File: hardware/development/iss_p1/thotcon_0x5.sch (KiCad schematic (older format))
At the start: 69 parts, among them J1 POWER, J2 ANALOG, J3 DIGITAL_0, J4 DIGITAL_1, J5 EXT_POWER, J6 USB_IN, P2 ICSP, U1 ATMEGA32U4, U2 5V, U3 3.3V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

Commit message: Apr 1 2014 Paul Reich
ANGES:
   Move R14 (2.2K TH) from add-on kit to production; USB needed on all models.

DELETIONS:
   prototype directory: Schematic obsolete. Refer instead to
   hardware/development/iss_P1/release/thotcon_0x5_SCHEM-*.pdf
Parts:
- R14: ASSY_STATUS DO NOT PLACE -> (none); Y (none) -> DO NOT PLACE
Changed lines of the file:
@@
 Sheet 1 1
 Title "BOARD, PC, THOTCON-0x05"
-Date "31 mar 2014"
+Date "1 apr 2014"
 Rev "P1"
 Comp "Workshop 88"
@@
 F 6 "CF18JT2K20" H 9150 7200 60  0001 C CNN "MFR_PN"
 F 7 ".02" H 9150 7200 60  0001 C CNN "EST_COST"
-F 8 "DO NOT PLACE" H 9150 7200 60  0001 C CNN "ASSY_STATUS"
+F 8 "DO NOT PLACE" H 9150 7200 60  0001 C CNN "Y"
 F 9 "Digi CF18JT2K20CT-ND" H 9150 7200 60  0001 C CNN "SUPPLIER_1"
 	1    9150 7200
@@
 83 FD EC 09 02 00 80 02 24 41 00 40 D7 20 09 02 00 BA 06 49 10 00 D0 35 48 82 00 80 AE 41 12 04
 00 74 0D 3E 91 01 00 74 0D 2A 41 00 40 D7 20 09 02 00 BA 06 49 10 00 D0 35 48 82 00 80 AE 41 12
-04 00 74 CD 7F 86 5F B2 B6 F3 AC DA 73 00 00 00 00 49 45 4E 44 AE 42 60 82 78 $EndBitmap
+04 00 74 CD 7F 86 5F B2 B6 F3 AC DA 73 00 00 00 00 49 45 4E 44 AE 42 60 82 43 $EndBitmap
 EndData
 $EndBitmap

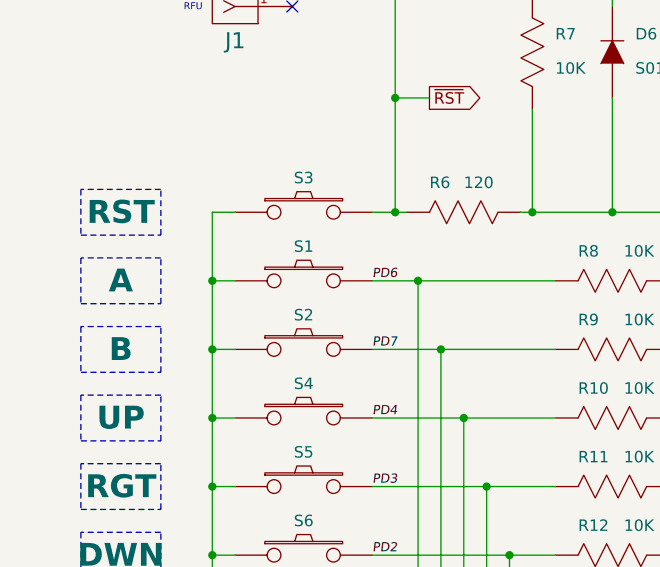
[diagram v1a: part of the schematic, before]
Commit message: April 11 2014 Paul Reich
Update schmatic/PCB information for pushbutton switches S1-S7. Do not
require the use of white display backing tape for certain silkscreen
colors (made possible by the use of a white-backed display).

Update assembly drawings and instructions accordingly.

Paul Reich
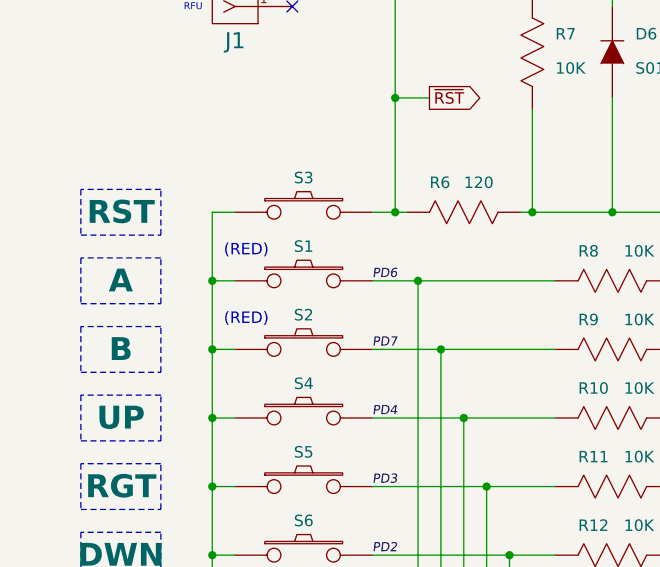
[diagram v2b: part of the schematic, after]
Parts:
- S1, S2: DESCRIPTION SW PB N.O. -> SW PB RED; EST_COST .35 -> .08; MFR OMRON -> TE CONN; MFR_PN B3F-1000 -> 1825910-7; NOTE (none) -> RED button; SUPPLIER_1 Mous 653-B3F-1000 -> (none); SUPPLIER_2 Digi SW400-ND -> Digi 450-1804-ND
- S3, S5, S7: DESCRIPTION SW PB N.O. -> SW PB BLACK; EST_COST .35 -> .08; MFR OMRON -> TE CONN; MFR_PN B3F-1000 -> FSM4JH; NOTE (none) -> BLACK button; SUPPLIER_1 Mous 653-B3F-1000 -> Mous 506-FSM4JH; SUPPLIER_2 Digi SW400-ND -> Digi 450-1650-ND
- S4: DESCRIPTION SW PB N.O. -> SW PB BLACK; EST_COST .35 -> .08; MFR OMRON -> TE CONN; MFR_PN B3F-1000 -> FSM4JH; SUPPLIER_1 Mous 653-B3F-1000 -> Mous 506-FSM4JH; SUPPLIER_2 Digi SW400-ND -> Digi 450-1650-ND
- S6: DESCRIPTION SW PB N.O. -> SW PB BLACK; EST_COST .35 -> .08; MFR OMRON -> TE CONN; MFR_PN B3F-1000 -> FSM4JH; NOTE (none) -> BLACK BUTTON; SUPPLIER_1 Mous 653-B3F-1000 -> Mous 506-FSM4JH; SUPPLIER_2 Digi SW400-ND -> Digi 450-1650-ND
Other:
- note added: "(RED)"
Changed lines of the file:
@@
 Sheet 1 1
 Title "BOARD, PC, THOTCON-0x05"
-Date "1 apr 2014"
+Date "11 apr 2014"
 Rev "P1"
 Comp "Workshop 88"
@@
 F 2 "PB_NO_6x6" H 1150 5750 100 0001 C CNN
 F 3 "" H 2000 5600 60  0001 C CNN
-F 4 "SW PB N.O." H 2000 5600 60  0001 C CNN "DESCRIPTION"
-F 5 "OMRON" H 2000 5600 60  0001 C CNN "MFR"
-F 6 "B3F-1000" H 2000 5600 60  0001 C CNN "MFR_PN"
-F 7 ".35" H 2000 5600 60  0001 C CNN "EST_COST"
+F 4 "SW PB BLACK" H 2000 5600 60  0001 C CNN "DESCRIPTION"
+F 5 "TE CONN" H 2000 5600 60  0001 C CNN "MFR"
+F 6 "FSM4JH" H 2000 5600 60  0001 C CNN "MFR_PN"
+F 7 ".08" H 2000 5600 60  0001 C CNN "EST_COST"
 F 8 "Y" H 2000 5600 60  0001 C CNN "ASSY_STATUS"
-F 9 "Mous 653-B3F-1000" H 2000 5600 60  0001 C CNN "SUPPLIER_1"
-F 10 "Digi SW400-ND" H 2000 5600 60  0001 C CNN "SUPPLIER_2"
+F 9 "Mous 506-FSM4JH" H 2000 5600 60  0001 C CNN "SUPPLIER_1"
+F 10 "Digi 450-1650-ND" H 2000 5600 60  0001 C CNN "SUPPLIER_2"
+F 11 "BLACK button" H 2000 5600 60  0001 C CNN "NOTE"
 	1    2000 5600
 	1    0    0    -1
@@
 D1 87 F9 97 3B 53 A9 15 6B BF 3C 0B 6E 5F 9C E9 E3 B9 64 B5 62 C1 87 F1 97 4B 37 64 C6 23 F2 D5
 BB 00 63 B1 AE 6B 50 C6 FB FD DE F7 BD 77 71 0C C3 30 EE C4 FF 44 53 4C EE 56 D8 FF 8A 00 00 00
-00 49 45 4E 44 AE 42 60 82 00 $EndBitmap
+00 49 45 4E 44 AE 42 60 82 13 $EndBitmap
 EndData
 $EndBitmap
@@
 F 2 "PB_NO_6x6" H 1150 6050 100 0001 C CNN
 F 3 "" H 2000 5900 60  0001 C CNN
-F 4 "SW PB N.O." H 2000 5900 60  0001 C CNN "DESCRIPTION"
-F 5 "OMRON" H 2000 5900 60  0001 C CNN "MFR"
-F 6 "B3F-1000" H 2000 5900 60  0001 C CNN "MFR_PN"
-F 7 ".35" H 2000 5900 60  0001 C CNN "EST_COST"
+F 4 "SW PB RED" H 2000 5900 60  0001 C CNN "DESCRIPTION"
+F 5 "TE CONN" H 2000 5900 60  0001 C CNN "MFR"
+F 6 "1825910-7" H 2000 5900 60  0001 C CNN "MFR_PN"
+F 7 ".08" H 2000 5900 60  0001 C CNN "EST_COST"
 F 8 "Y" H 2000 5900 60  0001 C CNN "ASSY_STATUS"
-F 9 "Mous 653-B3F-1000" H 2000 5900 60  0001 C CNN "SUPPLIER_1"
-F 10 "Digi SW400-ND" H 2000 5900 60  0001 C CNN "SUPPLIER_2"
+F 9 "Digi 450-1804-ND" H 2000 5900 60  0001 C CNN "SUPPLIER_2"
+F 10 "RED button" H 2000 5900 60  0001 C CNN "NOTE"
 	1    2000 5900
 	1    0    0    -1
@@
 F 2 "PB_NO_6x6" H 1150 6350 100 0001 C CNN
 F 3 "" H 2000 6200 60  0001 C CNN
-F 4 "SW PB N.O." H 2000 6200 60  0001 C CNN "DESCRIPTION"
-F 5 "OMRON" H 2000 6200 60  0001 C CNN "MFR"
-F 6 "B3F-1000" H 2000 6200 60  0001 C CNN "MFR_PN"
-F 7 ".35" H 2000 6200 60  0001 C CNN "EST_COST"
+F 4 "SW PB RED" H 2000 6200 60  0001 C CNN "DESCRIPTION"
+F 5 "TE CONN" H 2000 6200 60  0001 C CNN "MFR"
+F 6 "1825910-7" H 2000 6200 60  0001 C CNN "MFR_PN"
+F 7 ".08" H 2000 6200 60  0001 C CNN "EST_COST"
 F 8 "Y" H 2000 6200 60  0001 C CNN "ASSY_STATUS"
-F 9 "Mous 653-B3F-1000" H 2000 6200 60  0001 C CNN "SUPPLIER_1"
-F 10 "Digi SW400-ND" H 2000 6200 60  0001 C CNN "SUPPLIER_2"
+F 9 "Digi 450-1804-ND" H 2000 6200 60  0001 C CNN "SUPPLIER_2"
+F 10 "RED button" H 2000 6200 60  0001 C CNN "NOTE"
 	1    2000 6200
 	1    0    0    -1
@@
 F 2 "PB_NO_6x6" H 1150 6650 100 0001 C CNN
 F 3 "" H 2000 6500 60  0001 C CNN
-F 4 "SW PB N.O." H 2000 6500 60  0001 C CNN "DESCRIPTION"
-F 5 "OMRON" H 2000 6500 60  0001 C CNN "MFR"
-F 6 "B3F-1000" H 2000 6500 60  0001 C CNN "MFR_PN"
-F 7 ".35" H 2000 6500 60  0001 C CNN "EST_COST"
+F 4 "SW PB BLACK" H 2000 6500 60  0001 C CNN "DESCRIPTION"
+F 5 "TE CONN" H 2000 6500 60  0001 C CNN "MFR"
+F 6 "FSM4JH" H 2000 6500 60  0001 C CNN "MFR_PN"
+F 7 ".08" H 2000 6500 60  0001 C CNN "EST_COST"
 F 8 "Y" H 2000 6500 60  0001 C CNN "ASSY_STATUS"
-F 9 "Mous 653-B3F-1000" H 2000 6500 60  0001 C CNN "SUPPLIER_1"
-F 10 "Digi SW400-ND" H 2000 6500 60  0001 C CNN "SUPPLIER_2"
+F 9 "Mous 506-FSM4JH" H 2000 6500 60  0001 C CNN "SUPPLIER_1"
+F 10 "Digi 450-1650-ND" H 2000 6500 60  0001 C CNN "SUPPLIER_2"
 	1    2000 6500
 	1    0    0    -1
@@
 F 2 "PB_NO_6x6" H 1150 6950 100 0001 C CNN
 F 3 "" H 2000 6800 60  0001 C CNN
-F 4 "SW PB N.O." H 2000 6800 60  0001 C CNN "DESCRIPTION"
-F 5 "OMRON" H 2000 6800 60  0001 C CNN "MFR"
-F 6 "B3F-1000" H 2000 6800 60  0001 C CNN "MFR_PN"
-F 7 ".35" H 2000 6800 60  0001 C CNN "EST_COST"
+F 4 "SW PB BLACK" H 2000 6800 60  0001 C CNN "DESCRIPTION"
+F 5 "TE CONN" H 2000 6800 60  0001 C CNN "MFR"
+F 6 "FSM4JH" H 2000 6800 60  0001 C CNN "MFR_PN"
+F 7 ".08" H 2000 6800 60  0001 C CNN "EST_COST"
 F 8 "Y" H 2000 6800 60  0001 C CNN "ASSY_STATUS"
-F 9 "Mous 653-B3F-1000" H 2000 6800 60  0001 C CNN "SUPPLIER_1"
-F 10 "Digi SW400-ND" H 2000 6800 60  0001 C CNN "SUPPLIER_2"
+F 9 "Mous 506-FSM4JH" H 2000 6800 60  0001 C CNN "SUPPLIER_1"
+F 10 "Digi 450-1650-ND" H 2000 6800 60  0001 C CNN "SUPPLIER_2"
+F 11 "BLACK button" H 2000 6800 60  0001 C CNN "NOTE"
 	1    2000 6800
 	1    0    0    -1
@@
 F 2 "PB_NO_6x6" H 1150 7250 100 0001 C CNN
 F 3 "" H 2000 7100 60  0001 C CNN
-F 4 "SW PB N.O." H 2000 7100 60  0001 C CNN "DESCRIPTION"
-F 5 "OMRON" H 2000 7100 60  0001 C CNN "MFR"
-F 6 "B3F-1000" H 2000 7100 60  0001 C CNN "MFR_PN"
-F 7 ".35" H 2000 7100 60  0001 C CNN "EST_COST"
+F 4 "SW PB BLACK" H 2000 7100 60  0001 C CNN "DESCRIPTION"
+F 5 "TE CONN" H 2000 7100 60  0001 C CNN "MFR"
+F 6 "FSM4JH" H 2000 7100 60  0001 C CNN "MFR_PN"
+F 7 ".08" H 2000 7100 60  0001 C CNN "EST_COST"
 F 8 "Y" H 2000 7100 60  0001 C CNN "ASSY_STATUS"
-F 9 "Mous 653-B3F-1000" H 2000 7100 60  0001 C CNN "SUPPLIER_1"
-F 10 "Digi SW400-ND" H 2000 7100 60  0001 C CNN "SUPPLIER_2"
+F 9 "Mous 506-FSM4JH" H 2000 7100 60  0001 C CNN "SUPPLIER_1"
+F 10 "Digi 450-1650-ND" H 2000 7100 60  0001 C CNN "SUPPLIER_2"
+F 11 "BLACK BUTTON" H 2000 7100 60  0001 C CNN "NOTE"
 	1    2000 7100
 	1    0    0    -1
@@
 F 2 "PB_NO_6x6" H 1150 7550 100 0001 C CNN
 F 3 "" H 2000 7400 60  0001 C CNN
-F 4 "SW PB N.O." H 2000 7400 60  0001 C CNN "DESCRIPTION"
-F 5 "OMRON" H 2000 7400 60  0001 C CNN "MFR"
-F 6 "B3F-1000" H 2000 7400 60  0001 C CNN "MFR_PN"
-F 7 ".35" H 2000 7400 60  0001 C CNN "EST_COST"
+F 4 "SW PB BLACK" H 2000 7400 60  0001 C CNN "DESCRIPTION"
+F 5 "TE CONN" H 2000 7400 60  0001 C CNN "MFR"
+F 6 "FSM4JH" H 2000 7400 60  0001 C CNN "MFR_PN"
+F 7 ".08" H 2000 7400 60  0001 C CNN "EST_COST"
 F 8 "Y" H 2000 7400 60  0001 C CNN "ASSY_STATUS"
-F 9 "Mous 653-B3F-1000" H 2000 7400 60  0001 C CNN "SUPPLIER_1"
-F 10 "Digi SW400-ND" H 2000 7400 60  0001 C CNN "SUPPLIER_2"
+F 9 "Mous 506-FSM4JH" H 2000 7400 60  0001 C CNN "SUPPLIER_1"
+F 10 "Digi 450-1650-ND" H 2000 7400 60  0001 C CNN "SUPPLIER_2"
+F 11 "BLACK button" H 2000 7400 60  0001 C CNN "NOTE"
 	1    2000 7400
 	1    0    0    -1
@@
 83 FD EC 09 02 00 80 02 24 41 00 40 D7 20 09 02 00 BA 06 49 10 00 D0 35 48 82 00 80 AE 41 12 04
 00 74 0D 3E 91 01 00 74 0D 2A 41 00 40 D7 20 09 02 00 BA 06 49 10 00 D0 35 48 82 00 80 AE 41 12
-04 00 74 CD 7F 86 5F B2 B6 F3 AC DA 73 00 00 00 00 49 45 4E 44 AE 42 60 82 43 $EndBitmap
+04 00 74 CD 7F 86 5F B2 B6 F3 AC DA 73 00 00 00 00 49 45 4E 44 AE 42 60 82 01 $EndBitmap
 EndData
 $EndBitmap
@@
 Wire Notes Line
 	12950 700  16550 700
+Text Notes 1650 5800 0    50   ~ 0
+(RED)
+Text Notes 1650 6100 0    50   ~ 0
+(RED)
 $EndSCHEMATC
